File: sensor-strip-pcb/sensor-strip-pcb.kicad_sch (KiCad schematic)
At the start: 13 parts, among them J1 LED_Strip, J10 Arduino_Strip_Vin_Header, J11 Arduino_Strip_Vin_Terminal, J2 Left_Colour_Sensor, J3 Right_Colour_Sensor, J4 Red_Right_Detect_Pin, J5 Blue_Right_Detect_Pin, J6 Red_Left_Detect_Pin, J7 Blue_Left_Detect_Pin, J8 Right_Enable_Pin, J9 Left_Enable_Pin

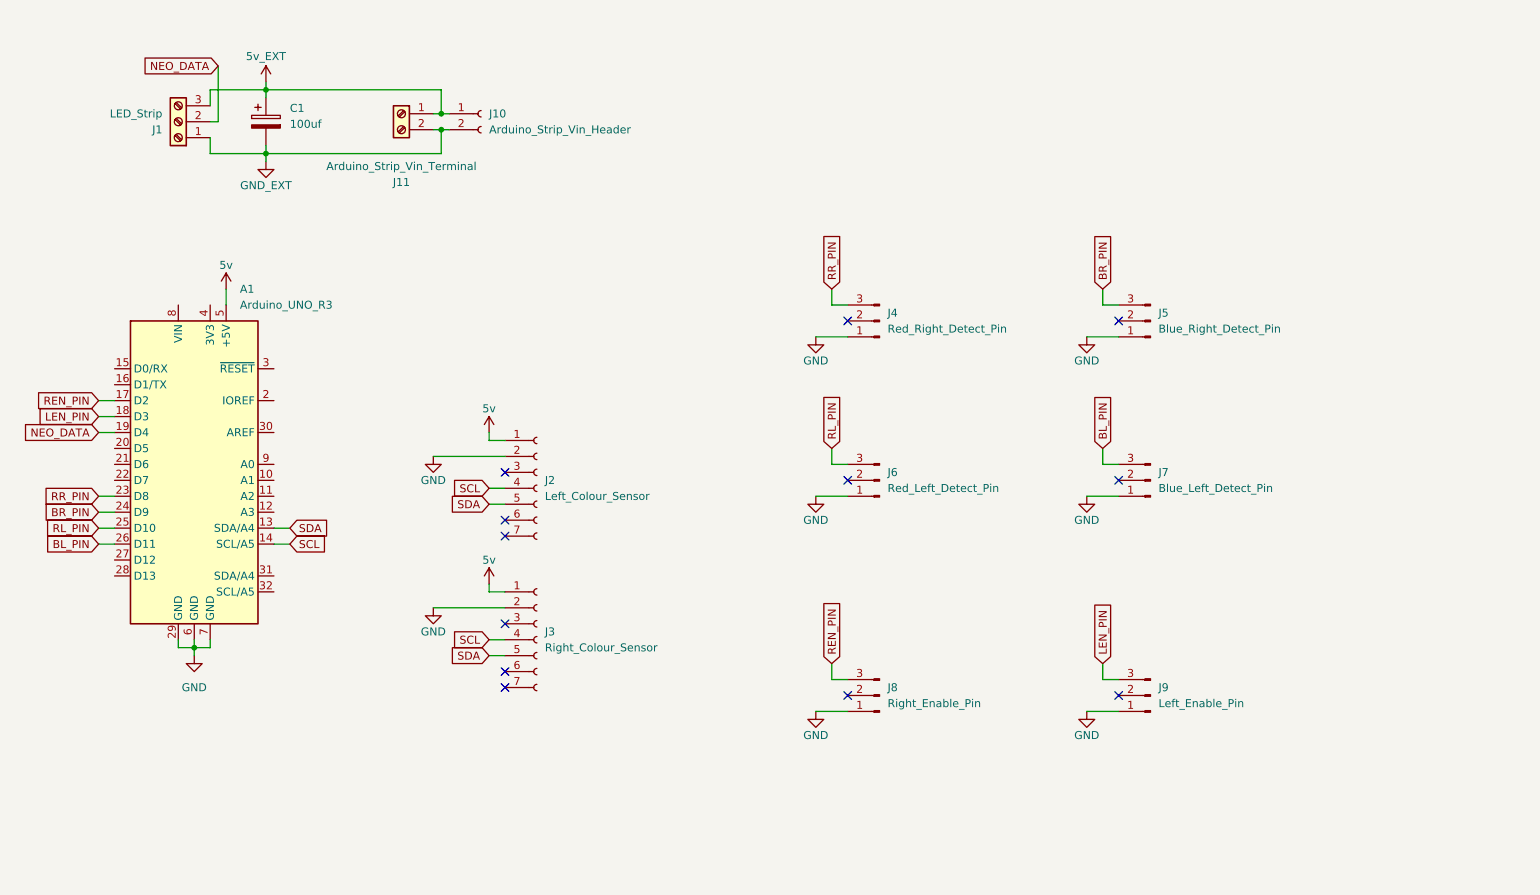
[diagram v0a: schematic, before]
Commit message: Finalized layout and trace routing
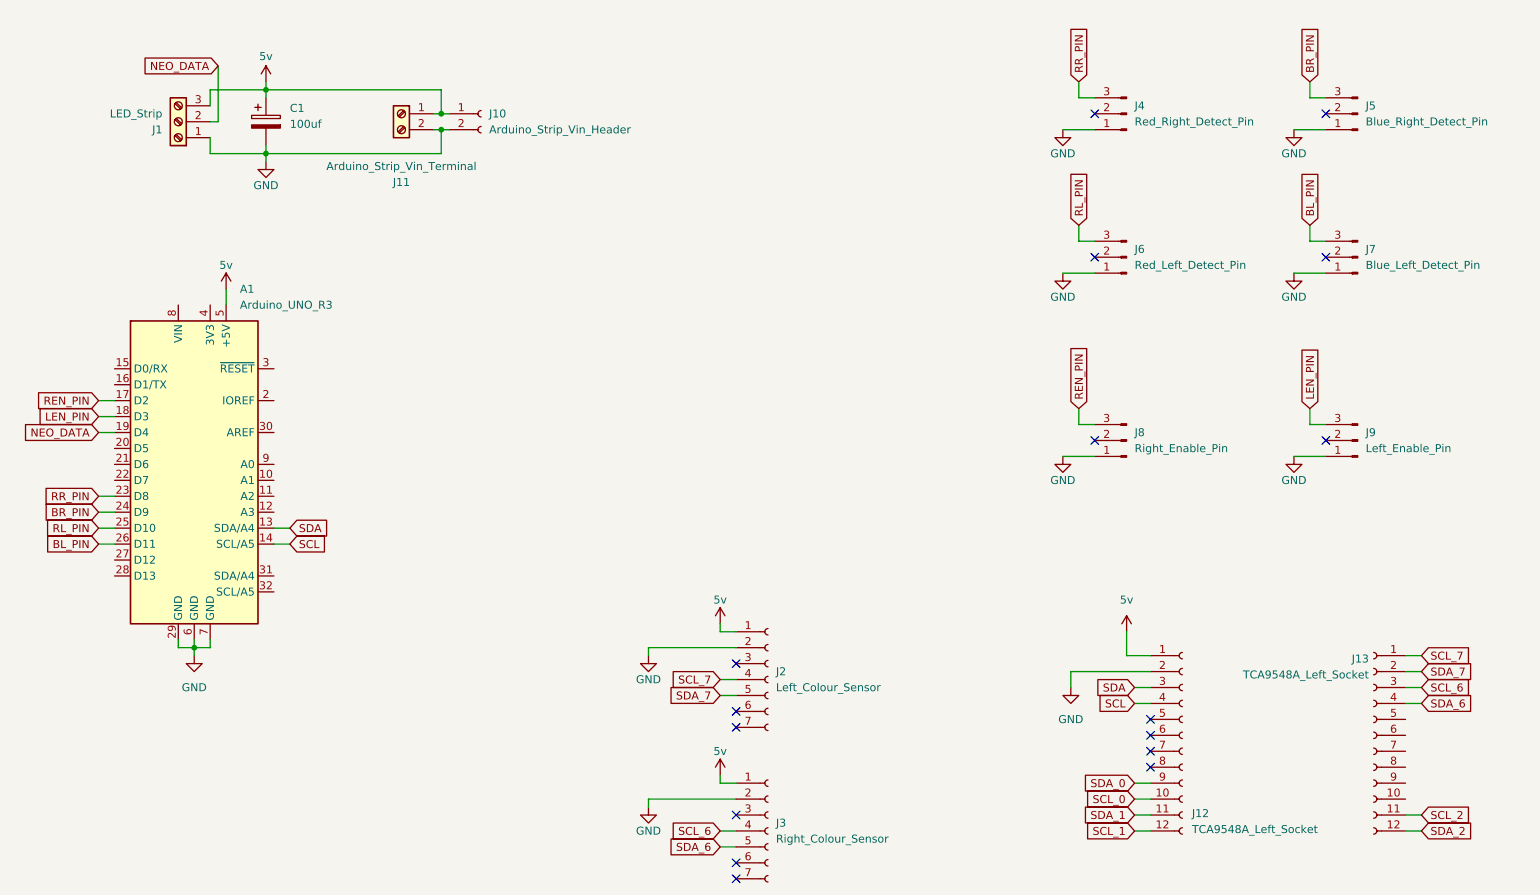
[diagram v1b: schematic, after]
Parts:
- added J12, J13: TCA9548A_Left_Socket, Connector_PinSocket_2.54mm:PinSocket_1x12_P2.54mm_Vertical, symbol Connector:Conn_01x12_Socket
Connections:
- net 5v_EXT is gone; now on net 5v: C1.1, J1.3 (Pin_3), J10.1 (Pin_1), J11.1 (Pin_1)
- net GND_EXT is gone; now on net GND: C1.2, J1.1 (Pin_1), J10.2 (Pin_2), J11.2 (Pin_2)
- net 5v: now also J12.1 (Pin_1)
- net GND: now also J12.2 (Pin_2)
- net SCL: now also J12.4 (Pin_4); no longer J2.4 (Pin_4), J3.4 (Pin_4)
- net SDA: now also J12.3 (Pin_3); no longer J2.5 (Pin_5), J3.5 (Pin_5)
- new net SCL_0: J12.10 (Pin_10)
- new net SCL_1: J12.12 (Pin_12)
- new net SCL_2: J13.11 (Pin_11)
- new net SCL_6: J13.3 (Pin_3), J3.4 (Pin_4)
- new net SCL_7: J13.1 (Pin_1), J2.4 (Pin_4)
- new net SDA_0: J12.9 (Pin_9)
- new net SDA_1: J12.11 (Pin_11)
- new net SDA_2: J13.12 (Pin_12)
- new net SDA_6: J13.4 (Pin_4), J3.5 (Pin_5)
- new net SDA_7: J13.2 (Pin_2), J2.5 (Pin_5)
- no-connect marks 12 -> 16
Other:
- moved on the sheet: J2, J3, J4, J5, J6, J7, J8, J9

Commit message: Finished silkscreen, finalized v1
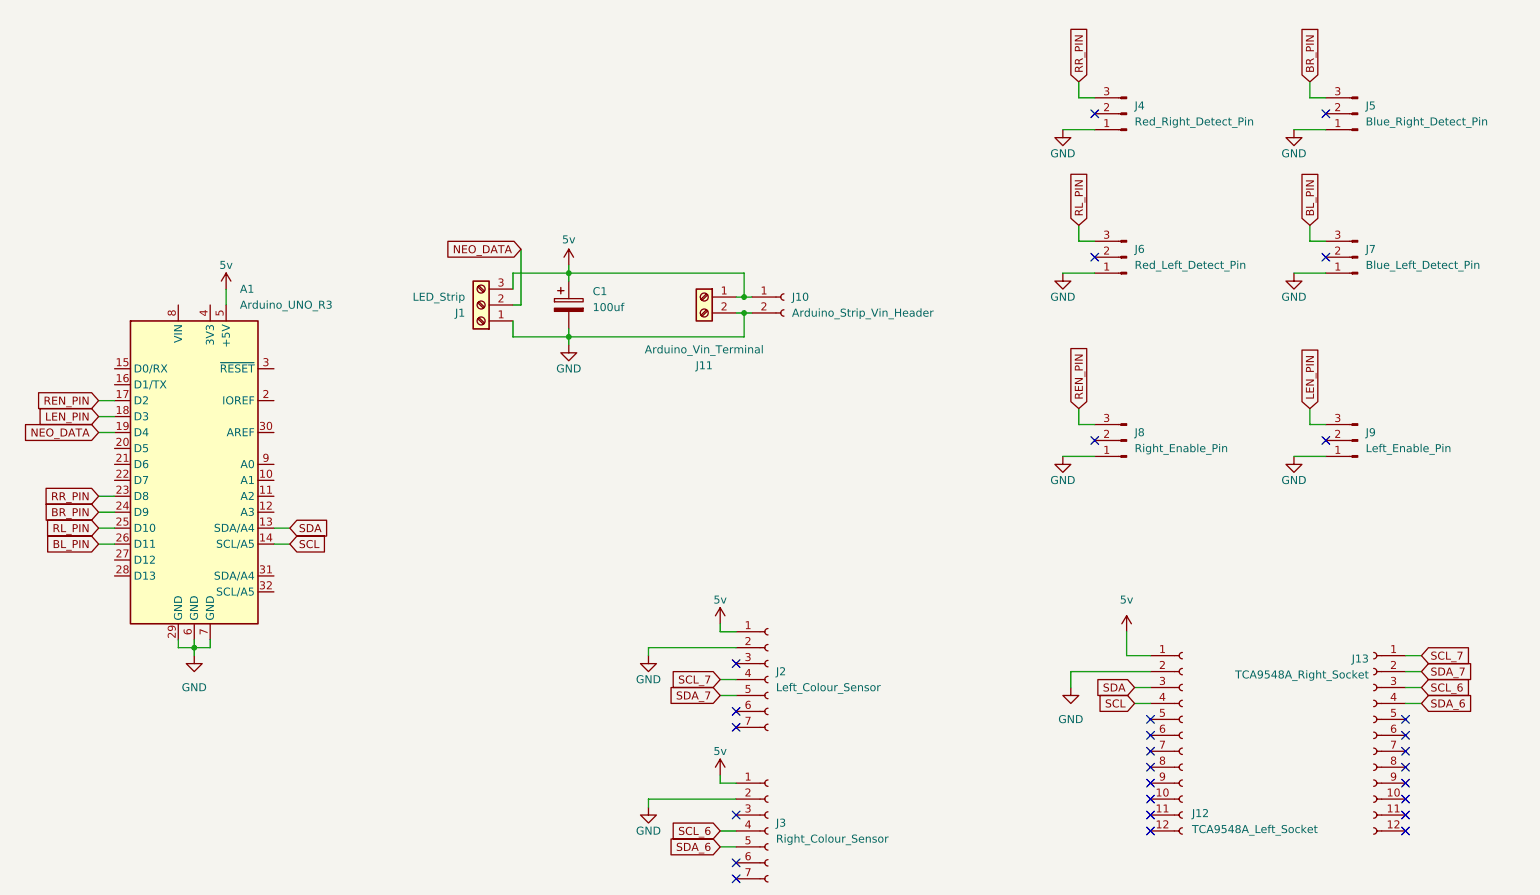
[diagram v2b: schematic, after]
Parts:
- J11: value Arduino_Strip_Vin_Terminal -> Arduino_Vin_Terminal
- J13: value TCA9548A_Left_Socket -> TCA9548A_Right_Socket
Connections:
- net SCL_0: no longer names the net of J12.10 (Pin_10)
- net SCL_1: no longer names the net of J12.12 (Pin_12)
- net SCL_2: no longer names the net of J13.11 (Pin_11)
- net SDA_0: no longer names the net of J12.9 (Pin_9)
- net SDA_1: no longer names the net of J12.11 (Pin_11)
- net SDA_2: no longer names the net of J13.12 (Pin_12)
- no-connect marks 16 -> 28
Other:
- moved on the sheet: C1, J1, J10, J11
